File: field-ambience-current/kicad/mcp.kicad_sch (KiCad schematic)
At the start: 68 parts, among them SW10 Modifier CLEAR (12x12x7.3 SMD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, SW6 Modifier SHIFT (12x12x7.3 SMD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, SW7 Modifier HOLD (12x12x7.3 SMD-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, SW8 Modifier DRONE (12x12x7.3 SMD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, SW9 Modifier GENERATE (12x12x7.3 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, U10 PCA9685PW #2 (16-Ch I²C PWM, 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, U2 MCP23017-E/SS (I/O-Expander), U6 PCA9685PW (16-Ch I²C PWM LED-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

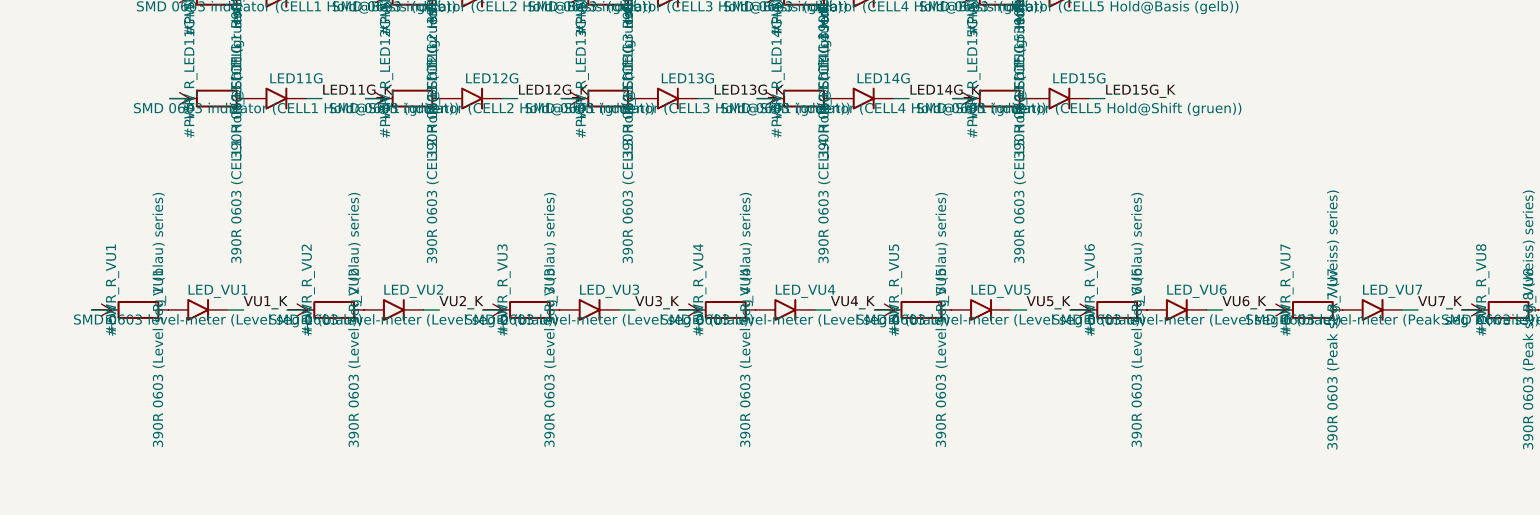
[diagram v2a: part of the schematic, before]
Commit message: parts: lock final part choices (button, VU white, side slide switch, headers) (#76)
* docs(pcb): completeness package — pinmap, JLC BOM export, handoff doc

Make the PCB design data component- and connectivity-complete so a PCB
engineer knows every pin / net / module without re-deriving from the
generator. Closes the gaps from the hardware gap analysis: the BOM alone
isn't production-ready, the generator is the source of truth, and the
pinmap / machine BOM / handoff package were missing.

New deliverables:
- docs/hardware/PINMAP.md — every STM32H743 LQFP-100 pin (all 100) → net →
  function/AF → module → external-component pin, plus per-module net tables
  (source → all sinks) for Power/MCU/LCD/MCP+LEDs/Encoders/Audio/Battery,
  and the verified free-pin list. Distilled from the generator NETS table.
- kicad/export_jlc_bom.py — stdlib-only JLC BOM exporter; parses the 7
  generated leaf .kicad_sch, skips #PWR + DNP, groups by LCSC, quotes
  comma-bearing values. Parts without LCSC go to a stderr NO-LCSC list
  (no guessing). Prints that CPL needs a routed .kicad_pcb (doesn't exist).
- kicad/jlc_bom.csv — generated: 57 LCSC parts, 188 placements.
- docs/hardware/PCB_HANDOFF.md — what's in the package, the engineer
  workflow, and the hard blockers before a fab order (ERC in GUI, layout +
  routing, mechanical coords, Gerber/CPL — all KiCad-GUI / user-side since
  there is no kicad-cli in this env).

Generator: swap LED6/LED7 physical colors to spec — Shift = gelb (C2287),
Hold = gruen (C12624) — attribute-only (same footprint/pads/net), so the
schematic, BOM and firmware are now consistent. Regenerated mcp.kicad_sch.

Also: PROJECT_STATUS r18.64 (1.9" display freeze, per-world musical
identity, Echo/Blur); MECHANICAL_REQUIREMENTS 1.9" freeze line;
component_reviews/README F-1/F-2/F-3 status corrections.

Docs/kicad/tools only — outside the firmware CI path filter.

Co-Authored-By: Claude Opus 4.8 <noreply@anthropic.com>
Claude-Session: https://claude.ai/code/session_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
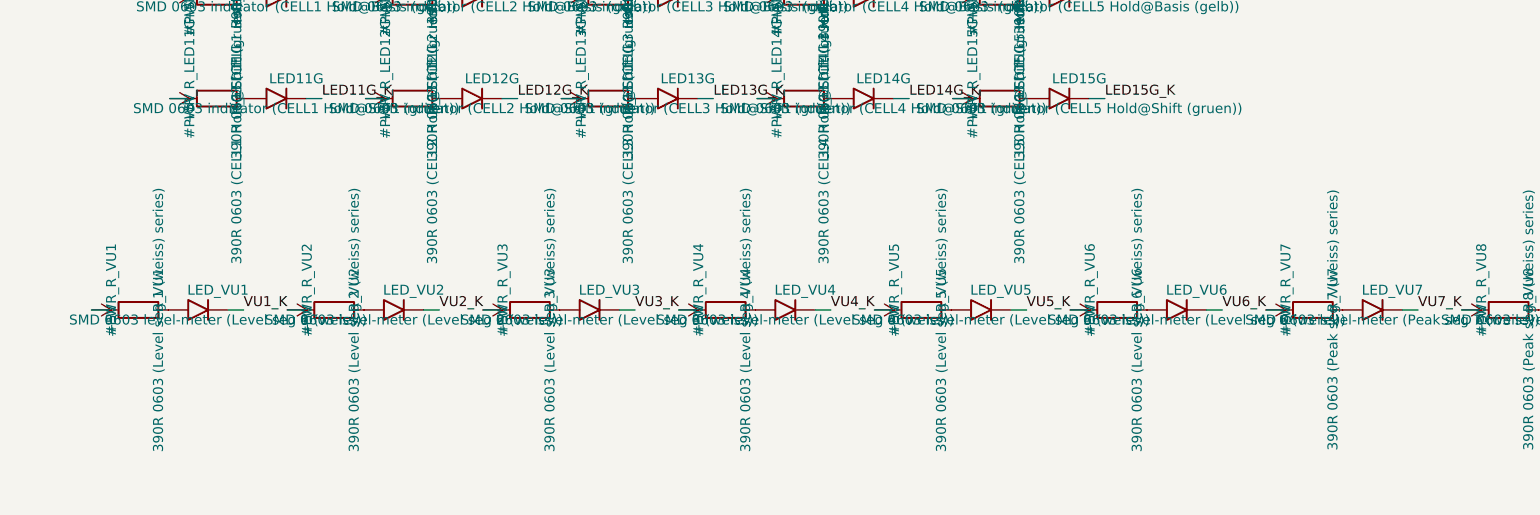
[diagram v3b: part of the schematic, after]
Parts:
- LED_VU1: value SMD 0603 level-meter (Level seg 1 (blau)) -> SMD 0603 level-meter (Level seg 1 (weiss)); LCSC (none) -> C965808; MPN KT-0603B (Hubei KENTO, blue 0603, Vf ~3.0V) — LCSC NEEDS-VE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 -> XL-1608UWC-04 (warm-white 0603)
- LED_VU2: value SMD 0603 level-meter (Level seg 2 (blau)) -> SMD 0603 level-meter (Level seg 2 (weiss)); LCSC (none) -> C965808; MPN KT-0603B (Hubei KENTO, blue 0603, Vf ~3.0V) — LCSC NEEDS-VE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 -> XL-1608UWC-04 (warm-white 0603)
- LED_VU3: value SMD 0603 level-meter (Level seg 3 (blau)) -> SMD 0603 level-meter (Level seg 3 (weiss)); LCSC (none) -> C965808; MPN KT-0603B (Hubei KENTO, blue 0603, Vf ~3.0V) — LCSC NEEDS-VE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 -> XL-1608UWC-04 (warm-white 0603)
- LED_VU4: value SMD 0603 level-meter (Level seg 4 (blau)) -> SMD 0603 level-meter (Level seg 4 (weiss)); LCSC (none) -> C965808; MPN KT-0603B (Hubei KENTO, blue 0603, Vf ~3.0V) — LCSC NEEDS-VE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 -> XL-1608UWC-04 (warm-white 0603)
- LED_VU5: value SMD 0603 level-meter (Level seg 5 (blau)) -> SMD 0603 level-meter (Level seg 5 (weiss)); LCSC (none) -> C965808; MPN KT-0603B (Hubei KENTO, blue 0603, Vf ~3.0V) — LCSC NEEDS-VE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 -> XL-1608UWC-04 (warm-white 0603)
- LED_VU6: value SMD 0603 level-meter (Level seg 6 (blau)) -> SMD 0603 level-meter (Level seg 6 (weiss)); LCSC (none) -> C965808; MPN KT-0603B (Hubei KENTO, blue 0603, Vf ~3.0V) — LCSC NEEDS-VE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 -> XL-1608UWC-04 (warm-white 0603)
- R_VU1: value 390R 0603 (Level seg 1 (blau) series) -> 390R 0603 (Level seg 1 (weiss) series)
- R_VU2: value 390R 0603 (Level seg 2 (blau) series) -> 390R 0603 (Level seg 2 (weiss) series)
- R_VU3: value 390R 0603 (Level seg 3 (blau) series) -> 390R 0603 (Level seg 3 (weiss) series)
- R_VU4: value 390R 0603 (Level seg 4 (blau) series) -> 390R 0603 (Level seg 4 (weiss) series)
- R_VU5: value 390R 0603 (Level seg 5 (blau) series) -> 390R 0603 (Level seg 5 (weiss) series)
- R_VU6: value 390R 0603 (Level seg 6 (blau) series) -> 390R 0603 (Level seg 6 (weiss) series)
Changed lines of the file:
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@@
     (comment 2 "MCP 0x20 / U6 PCA 0x40 / U10 PCA 0x41 (A0=+3V3) - shared I²C bus")
     (comment 3 "r10: SW6-SW10 plain HX 12x12x7.3TPFT-B SMD-Tactile (C36498966)")
-    (comment 4 "r10: 10× LEDs (LED6-LED15); U10 PCA9685 #2 -> 8 VU-Level-LEDs (blau+weiss)"))
+    (comment 4 "r10: 10× LEDs (LED6-LED15); U10 PCA9685 #2 -> 8 VU-Level-LEDs (weiss)"))
   (symbol (lib_id "MCU:MCP23017") (at 130.0 110.0 0) (unit 1)
     (in_bom yes) (on_board yes) (dnp no)
@@
       (property "Reference" "R_VU1" (at 72.54 252.46 0)
         (effects (font (size 1.27 1.27))))
-      (property "Value" "390R 0603 (Level seg 1 (blau) series)" (at 72.54 256.27 0)
+      (property "Value" "390R 0603 (Level seg 1 (weiss) series)" (at 72.54 256.27 0)
         (effects (font (size 1.27 1.27))))
       (property "Footprint" "Resistor_SMD:R_0603_1608Metric" (at 70 255 0)
@@
       (property "Reference" "LED_VU1" (at 80.16000000000001 252.46 0)
         (effects (font (size 1.27 1.27))))
-      (property "Value" "SMD 0603 level-meter (Level seg 1 (blau))" (at 80.16000000000001 256.27 0)
+      (property "Value" "SMD 0603 level-meter (Level seg 1 (weiss))" (at 80.16000000000001 256.27 0)
         (effects (font (size 1.27 1.27))))
       (property "Footprint" "LED_SMD:LED_0603_1608Metric" (at 77.62 255 0)
@@
       (property "Datasheet" "~" (at 77.62 255 0)
         (effects (font (size 1.27 1.27)) hide))
-      (property "MPN" "KT-0603B (Hubei KENTO, blue 0603, Vf ~3.0V) — LCSC NEEDS-VERIFY" (at 80.16000000000001 258.81 0)
-        (effects (font (size 1.27 1.27)) hide))
-      (property "LCSC" "" (at 80.16000000000001 260.08 0)
+      (property "MPN" "XL-1608UWC-04 (warm-white 0603)" (at 80.16000000000001 258.81 0)
+        (effects (font (size 1.27 1.27)) hide))
+      (property "LCSC" "C965808" (at 80.16000000000001 260.08 0)
         (effects (font (size 1.27 1.27)) hide))
     (instances
@@
       (property "Reference" "R_VU2" (at 97.54 252.46 0)
         (effects (font (size 1.27 1.27))))
-      (property "Value" "390R 0603 (Level seg 2 (blau) series)" (at 97.54 256.27 0)
+      (property "Value" "390R 0603 (Level seg 2 (weiss) series)" (at 97.54 256.27 0)
         (effects (font (size 1.27 1.27))))
       (property "Footprint" "Resistor_SMD:R_0603_1608Metric" (at 95 255 0)
@@
       (property "Reference" "LED_VU2" (at 105.16000000000001 252.46 0)
         (effects (font (size 1.27 1.27))))
-      (property "Value" "SMD 0603 level-meter (Level seg 2 (blau))" (at 105.16000000000001 256.27 0)
+      (property "Value" "SMD 0603 level-meter (Level seg 2 (weiss))" (at 105.16000000000001 256.27 0)
         (effects (font (size 1.27 1.27))))
       (property "Footprint" "LED_SMD:LED_0603_1608Metric" (at 102.62 255 0)
@@
       (property "Datasheet" "~" (at 102.62 255 0)
         (effects (font (size 1.27 1.27)) hide))
-      (property "MPN" "KT-0603B (Hubei KENTO, blue 0603, Vf ~3.0V) — LCSC NEEDS-VERIFY" (at 105.16000000000001 258.81 0)
-        (effects (font (size 1.27 1.27)) hide))
-      (property "LCSC" "" (at 105.16000000000001 260.08 0)
+      (property "MPN" "XL-1608UWC-04 (warm-white 0603)" (at 105.16000000000001 258.81 0)
+        (effects (font (size 1.27 1.27)) hide))
+      (property "LCSC" "C965808" (at 105.16000000000001 260.08 0)
         (effects (font (size 1.27 1.27)) hide))
     (instances
@@
       (property "Reference" "R_VU3" (at 122.54 252.46 0)
         (effects (font (size 1.27 1.27))))
-      (property "Value" "390R 0603 (Level seg 3 (blau) series)" (at 122.54 256.27 0)
+      (property "Value" "390R 0603 (Level seg 3 (weiss) series)" (at 122.54 256.27 0)
         (effects (font (size 1.27 1.27))))
       (property "Footprint" "Resistor_SMD:R_0603_1608Metric" (at 120 255 0)
@@
       (property "Reference" "LED_VU3" (at 130.16 252.46 0)
         (effects (font (size 1.27 1.27))))
-      (property "Value" "SMD 0603 level-meter (Level seg 3 (blau))" (at 130.16 256.27 0)
+      (property "Value" "SMD 0603 level-meter (Level seg 3 (weiss))" (at 130.16 256.27 0)
         (effects (font (size 1.27 1.27))))
       (property "Footprint" "LED_SMD:LED_0603_1608Metric" (at 127.62 255 0)
@@
       (property "Datasheet" "~" (at 127.62 255 0)
         (effects (font (size 1.27 1.27)) hide))
-      (property "MPN" "KT-0603B (Hubei KENTO, blue 0603, Vf ~3.0V) — LCSC NEEDS-VERIFY" (at 130.16 258.81 0)
-        (effects (font (size 1.27 1.27)) hide))
-      (property "LCSC" "" (at 130.16 260.08 0)
+      (property "MPN" "XL-1608UWC-04 (warm-white 0603)" (at 130.16 258.81 0)
+        (effects (font (size 1.27 1.27)) hide))
+      (property "LCSC" "C965808" (at 130.16 260.08 0)
         (effects (font (size 1.27 1.27)) hide))
     (instances
@@
       (property "Reference" "R_VU4" (at 147.54 252.46 0)
         (effects (font (size 1.27 1.27))))
-      (property "Value" "390R 0603 (Level seg 4 (blau) series)" (at 147.54 256.27 0)
+      (property "Value" "390R 0603 (Level seg 4 (weiss) series)" (at 147.54 256.27 0)
         (effects (font (size 1.27 1.27))))
       (property "Footprint" "Resistor_SMD:R_0603_1608Metric" (at 145 255 0)
@@
       (property "Reference" "LED_VU4" (at 155.16 252.46 0)
         (effects (font (size 1.27 1.27))))
-      (property "Value" "SMD 0603 level-meter (Level seg 4 (blau))" (at 155.16 256.27 0)
+      (property "Value" "SMD 0603 level-meter (Level seg 4 (weiss))" (at 155.16 256.27 0)
         (effects (font (size 1.27 1.27))))
       (property "Footprint" "LED_SMD:LED_0603_1608Metric" (at 152.62 255 0)
@@
       (property "Datasheet" "~" (at 152.62 255 0)
         (effects (font (size 1.27 1.27)) hide))
-      (property "MPN" "KT-0603B (Hubei KENTO, blue 0603, Vf ~3.0V) — LCSC NEEDS-VERIFY" (at 155.16 258.81 0)
-        (effects (font (size 1.27 1.27)) hide))
-      (property "LCSC" "" (at 155.16 260.08 0)
+      (property "MPN" "XL-1608UWC-04 (warm-white 0603)" (at 155.16 258.81 0)
+        (effects (font (size 1.27 1.27)) hide))
+      (property "LCSC" "C965808" (at 155.16 260.08 0)
         (effects (font (size 1.27 1.27)) hide))
     (instances
@@
       (property "Reference" "R_VU5" (at 172.54 252.46 0)
         (effects (font (size 1.27 1.27))))
-      (property "Value" "390R 0603 (Level seg 5 (blau) series)" (at 172.54 256.27 0)
+      (property "Value" "390R 0603 (Level seg 5 (weiss) series)" (at 172.54 256.27 0)
         (effects (font (size 1.27 1.27))))
       (property "Footprint" "Resistor_SMD:R_0603_1608Metric" (at 170 255 0)
@@
       (property "Reference" "LED_VU5" (at 180.16 252.46 0)
         (effects (font (size 1.27 1.27))))
-      (property "Value" "SMD 0603 level-meter (Level seg 5 (blau))" (at 180.16 256.27 0)
+      (property "Value" "SMD 0603 level-meter (Level seg 5 (weiss))" (at 180.16 256.27 0)
         (effects (font (size 1.27 1.27))))
       (property "Footprint" "LED_SMD:LED_0603_1608Metric" (at 177.62 255 0)
@@
       (property "Datasheet" "~" (at 177.62 255 0)
         (effects (font (size 1.27 1.27)) hide))
-      (property "MPN" "KT-0603B (Hubei KENTO, blue 0603, Vf ~3.0V) — LCSC NEEDS-VERIFY" (at 180.16 258.81 0)
-        (effects (font (size 1.27 1.27)) hide))
-      (property "LCSC" "" (at 180.16 260.08 0)
+      (property "MPN" "XL-1608UWC-04 (warm-white 0603)" (at 180.16 258.81 0)
+        (effects (font (size 1.27 1.27)) hide))
+      (property "LCSC" "C965808" (at 180.16 260.08 0)
         (effects (font (size 1.27 1.27)) hide))
     (instances
@@
       (property "Reference" "R_VU6" (at 197.54 252.46 0)
         (effects (font (size 1.27 1.27))))
-      (property "Value" "390R 0603 (Level seg 6 (blau) series)" (at 197.54 256.27 0)
+      (property "Value" "390R 0603 (Level seg 6 (weiss) series)" (at 197.54 256.27 0)
         (effects (font (size 1.27 1.27))))
       (property "Footprint" "Resistor_SMD:R_0603_1608Metric" (at 195 255 0)
@@
       (property "Reference" "LED_VU6" (at 205.16 252.46 0)
         (effects (font (size 1.27 1.27))))
-      (property "Value" "SMD 0603 level-meter (Level seg 6 (blau))" (at 205.16 256.27 0)
+      (property "Value" "SMD 0603 level-meter (Level seg 6 (weiss))" (at 205.16 256.27 0)
         (effects (font (size 1.27 1.27))))
       (property "Footprint" "LED_SMD:LED_0603_1608Metric" (at 202.62 255 0)
@@
       (property "Datasheet" "~" (at 202.62 255 0)
         (effects (font (size 1.27 1.27)) hide))
-      (property "MPN" "KT-0603B (Hubei KENTO, blue 0603, Vf ~3.0V) — LCSC NEEDS-VERIFY" (at 205.16 258.81 0)
-        (effects (font (size 1.27 1.27)) hide))
-      (property "LCSC" "" (at 205.16 260.08 0)
-        (effects (font (size 1.27 1.27)) hide))
-    (instances
+      (property "MPN" "XL-1608UWC-04 (warm-white 0603)" (at 205.16 258.81 0)
+        (effects (font (size 1.27 1.27)) hide))
+      (property "LCSC" "C965808" (at 205.16 260.08 0)
+        (effects (font (size 1.27 1.27)) hide))
+    (instances
